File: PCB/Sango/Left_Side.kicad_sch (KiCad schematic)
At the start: 38 parts, among them IC1 W25Q16JVUXIQ, J1 USB_C_Receptacle_USB2.0, J2 AudioJack4, SW1 SW_Push, U1 RP2040, U2 XC6210B332MR, U5 USBLC6-2P6, U6 USBLC6-2P6, Y1 Crystal_GND24

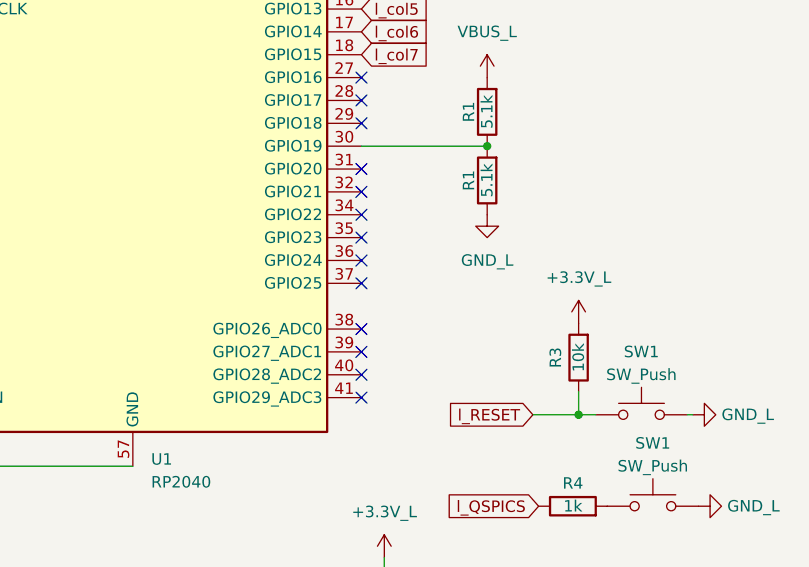
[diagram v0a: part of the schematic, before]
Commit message: Added handdedness pin (GPIO25).
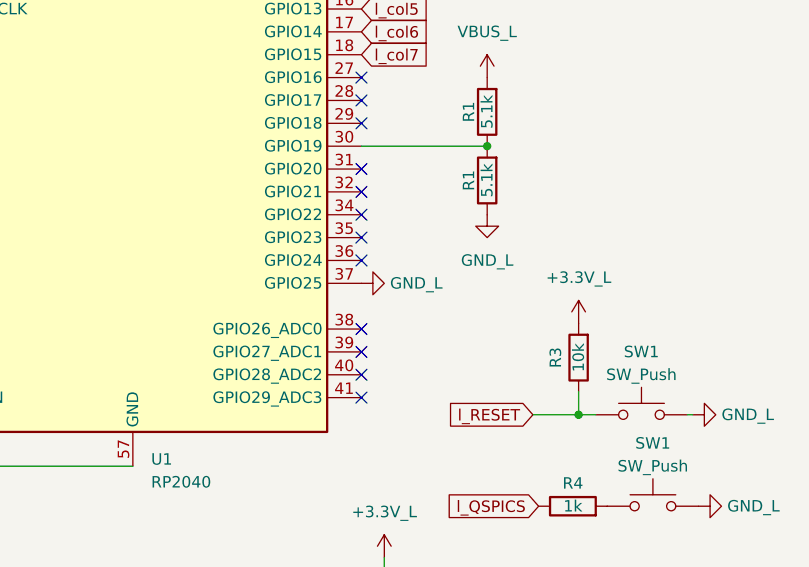
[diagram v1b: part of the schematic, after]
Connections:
- net GND_L: now also U1.37 (GPIO25)
- no-connect marks 21 -> 20
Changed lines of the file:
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@@
   (no_connect (at 181.61 96.52))
   (no_connect (at 232.41 106.68))
-  (no_connect (at 232.41 93.98))
   (no_connect (at 232.41 91.44))
   (no_connect (at 232.41 71.12))
@@
         )
       )
+    )
+  )
+  (symbol (lib_id "Aidans-Custom-Lib:GND_L") (at 232.41 93.98 90) (unit 1)
+    (in_bom yes) (on_board yes) (dnp no) (fields_autoplaced)
+    (property "Reference" "#PWR088" (at 238.76 93.98 0)
+      (effects (font (size 1.27 1.27)) hide)
+    )
+    (property "Value" "GND_L" (at 235.585 93.98 90)
+      (effects (font (size 1.27 1.27)) (justify right))
+    )
+    (property "Footprint" "" (at 232.41 93.98 0)
+      (effects (font (size 1.27 1.27)) hide)
+    )
+    (property "Datasheet" "" (at 232.41 93.98 0)
+      (effects (font (size 1.27 1.27)) hide)
+    )
+    (pin "1")
+    (instances
+      (project "Sango"
+        (path "/b3610507-f8cf-4536-91fb-ccd246b0546b/a7f827bb-7abe-440f-bda3-0d9b99750074"
+          (reference "#PWR088") (unit 1)
+        )
+      )
